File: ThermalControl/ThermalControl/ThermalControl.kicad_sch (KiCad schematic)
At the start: 24 parts, among them J1 12V, J2 GND, J3 DC-005, J4 5V, U1 NODE_MCU, U2 RLY_MD_SCKT_1CH

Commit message: project ready to production
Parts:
- removed R10, R8, R9: 1k, Resistor_THT:R_Axial_DIN0207_L6.3mm_D2.5mm_P7.62mm_Horizontal, symbol Device:R
- removed R6, R7: 330, Resistor_THT:R_Axial_DIN0207_L6.3mm_D2.5mm_P7.62mm_Horizontal, symbol Device:R
- R3: renamed from R11; value 1k -> 4.7K
- renumbered C2 to C1, C1 to C2, J4 to J1, J1 to J4, R2 to R1, R1 to R2, R3 to R5
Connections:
- net at C2.1, J1.1 (Pin_1), SENSOR1.3 (VDD)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: now also R3.2; no longer R3.1
- net at SENSOR1.2 (DQ), U1.28 (D2): now also R3.1
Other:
- company: (none) -> FeapTech
- title: (none) -> NodeMCU Thermal Control
- moved on the sheet: R3

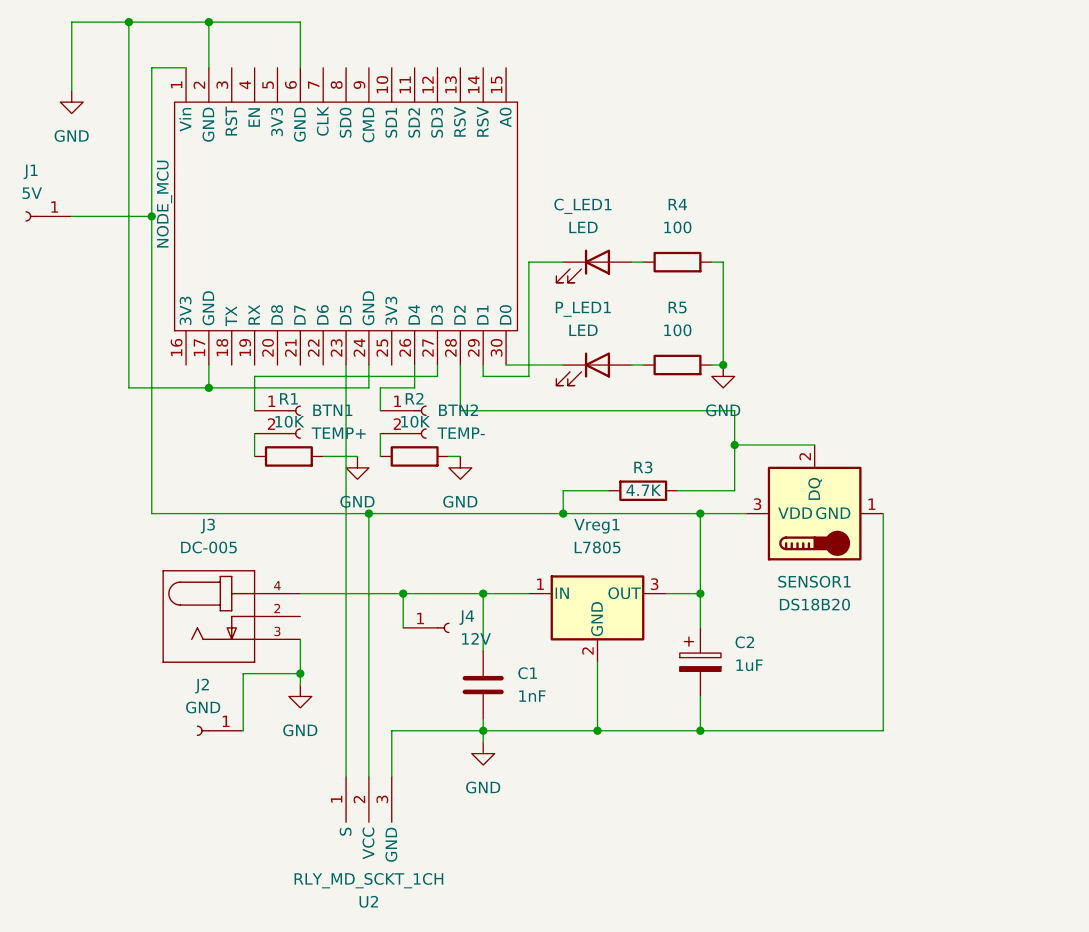
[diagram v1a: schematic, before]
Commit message: changed relay to mosfet
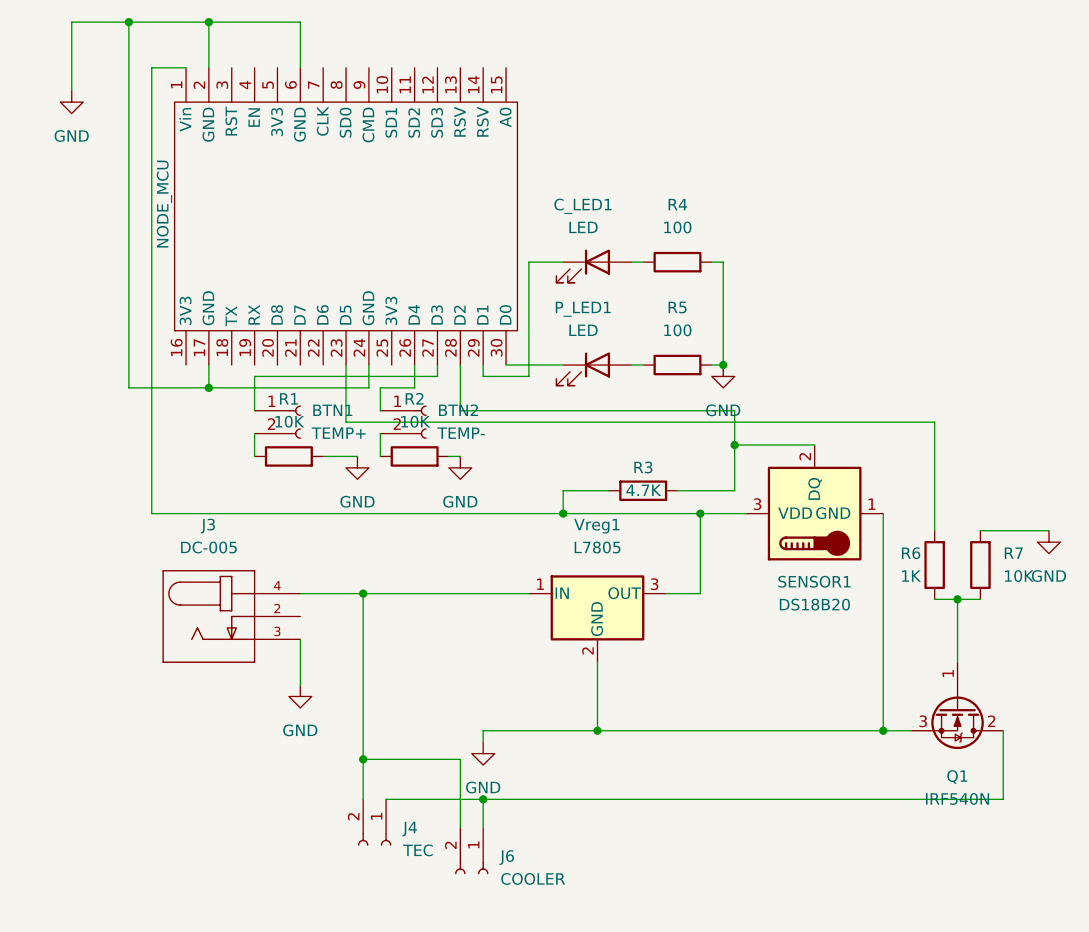
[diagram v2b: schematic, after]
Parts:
- removed C1: 1nF, Capacitor_THT:C_Disc_D5.0mm_W2.5mm_P5.00mm, symbol Device:C
- removed C2: 1uF, Capacitor_THT:CP_Radial_D5.0mm_P2.50mm, symbol Device:C_Polarized
- removed J1: 5V, Connector_PinHeader_1.27mm:PinHeader_1x01_P1.27mm_Vertical, symbol Connector:Conn_01x01_Female
- removed J2: GND, Connector_PinHeader_1.27mm:PinHeader_1x01_P1.27mm_Vertical, symbol Connector:Conn_01x01_Female
- removed J4: 12V, Connector_PinHeader_1.27mm:PinHeader_1x01_P1.27mm_Vertical, symbol Connector:Conn_01x01_Female
- removed U2: RLY_MD_SCKT_1CH, Connector:RELAY_MODULE_SOCKET_1CH, symbol relay_module:RLY_MD_SCKT_1CH
- added J4: TEC, Connector_Wire:SolderWire-0.5sqmm_1x02_P4.8mm_D0.9mm_OD2.3mm, symbol Connector:Conn_01x02_Female
- added J6: COOLER, Connector_Wire:SolderWire-0.5sqmm_1x02_P4.8mm_D0.9mm_OD2.3mm, symbol Connector:Conn_01x02_Female
- added Q1: IRF540N, Package_TO_SOT_THT:TO-220-3_Vertical, symbol Transistor_FET:IRF540N
- added R6: 1K, Resistor_THT:R_Axial_DIN0207_L6.3mm_D2.5mm_P7.62mm_Horizontal, symbol Device:R
- added R7: 10K, Resistor_THT:R_Axial_DIN0207_L6.3mm_D2.5mm_P7.62mm_Horizontal, symbol Device:R
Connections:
- net GND: now also Q1.3 (S), R7.2
- net at J3.4, Vreg1.1 (IN): now also J4.2 (Pin_2), J6.2 (Pin_2)
- net at U1.23 (D5): now also R6.2
- new net: J4.1 (Pin_1), J6.1 (Pin_1), Q1.2 (D)
- new net: Q1.1 (G), R6.1, R7.1
